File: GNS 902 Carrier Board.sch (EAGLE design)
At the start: 8 parts, among them U1 GNS-902

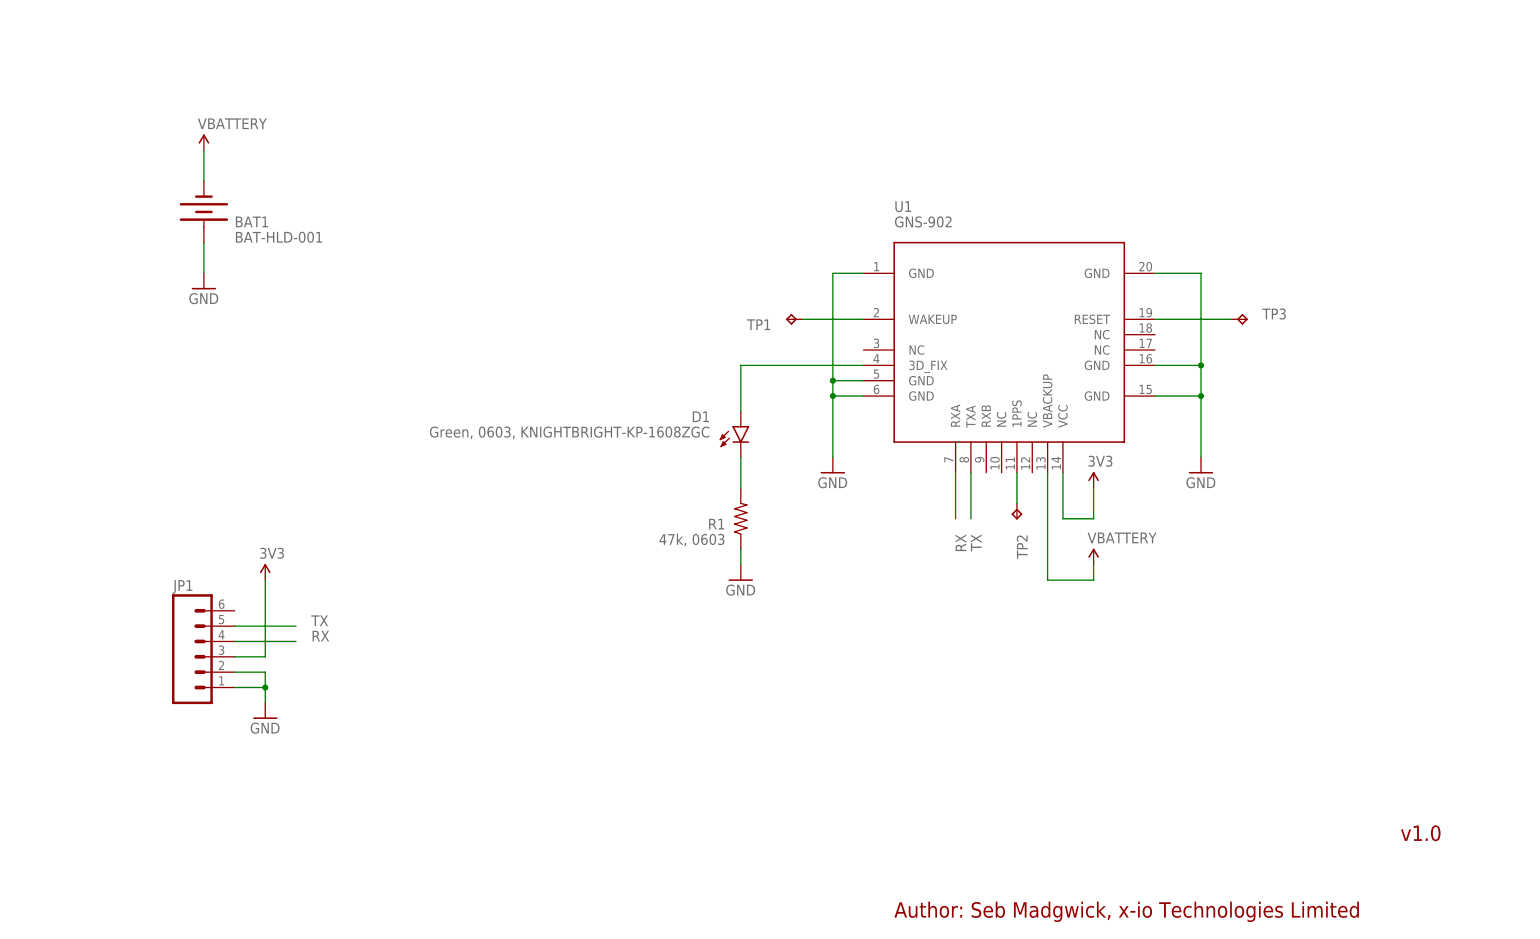
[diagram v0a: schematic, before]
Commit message: Add automatic VBACKUP power source switch
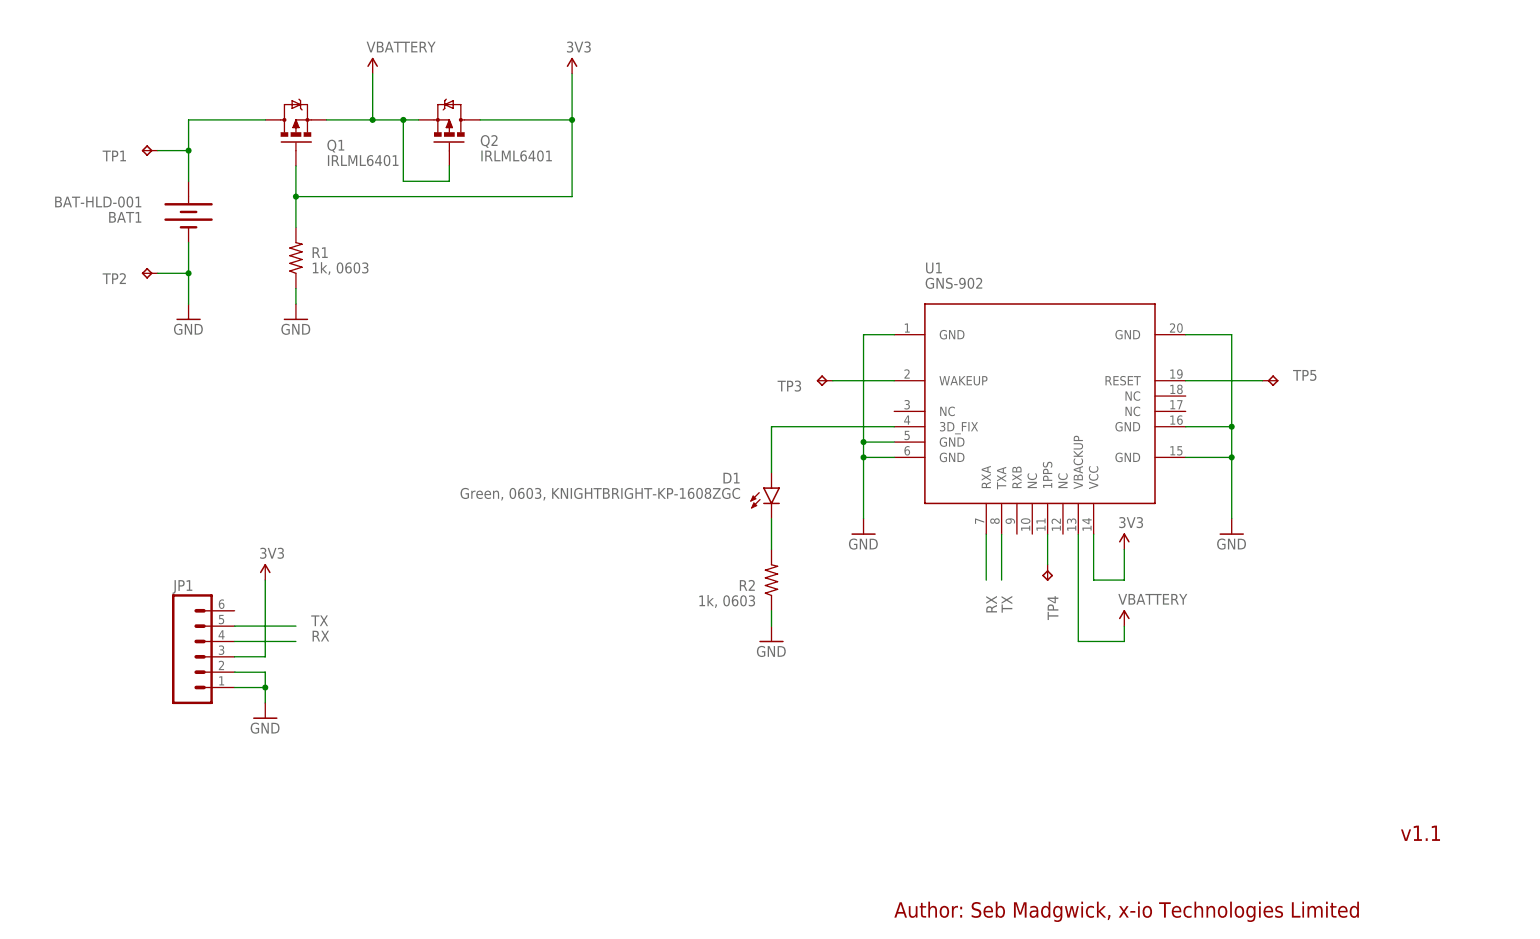
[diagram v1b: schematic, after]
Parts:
- added Q1, Q2: IRLML6401, SparkFun-DiscreteSemi:MOSFET-PCHANNEL
- added R2: 1k, 0603, SparkFun-Resistors:RESISTOR0603
- added TP4, TP5: TPTP10R, testpad:TPTP10R
- R1: value 47k, 0603 -> 1k, 0603
- TP1, TP2: value TPTP10R -> TPTP15R; device testpad:TPTP10R -> testpad:TPTP15R
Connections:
- new net N$6: BAT1.+, Q1.D, TP1.TP
- net 3V3: now also Q1.G, Q2.D, R1.2
- net GND: now also BAT1.-, R2.1, TP2.TP; no longer BAT1.+
- net N$2: now also R2.2; no longer R1.2
- net N$3: now also TP3.TP; no longer TP1.TP
- net N$4: now also TP4.TP; no longer TP2.TP
- net N$5: now also TP5.TP; no longer TP3.TP
- net VBATTERY: now also Q1.S, Q2.G, Q2.S; no longer BAT1.-
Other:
- note added: "v1.1"
- note removed: "v1.0"
- moved on the sheet: BAT1, D1, R1, TP1, TP2, TP3, U1

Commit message: Correct GNS-902 footprint and add notes to schematic
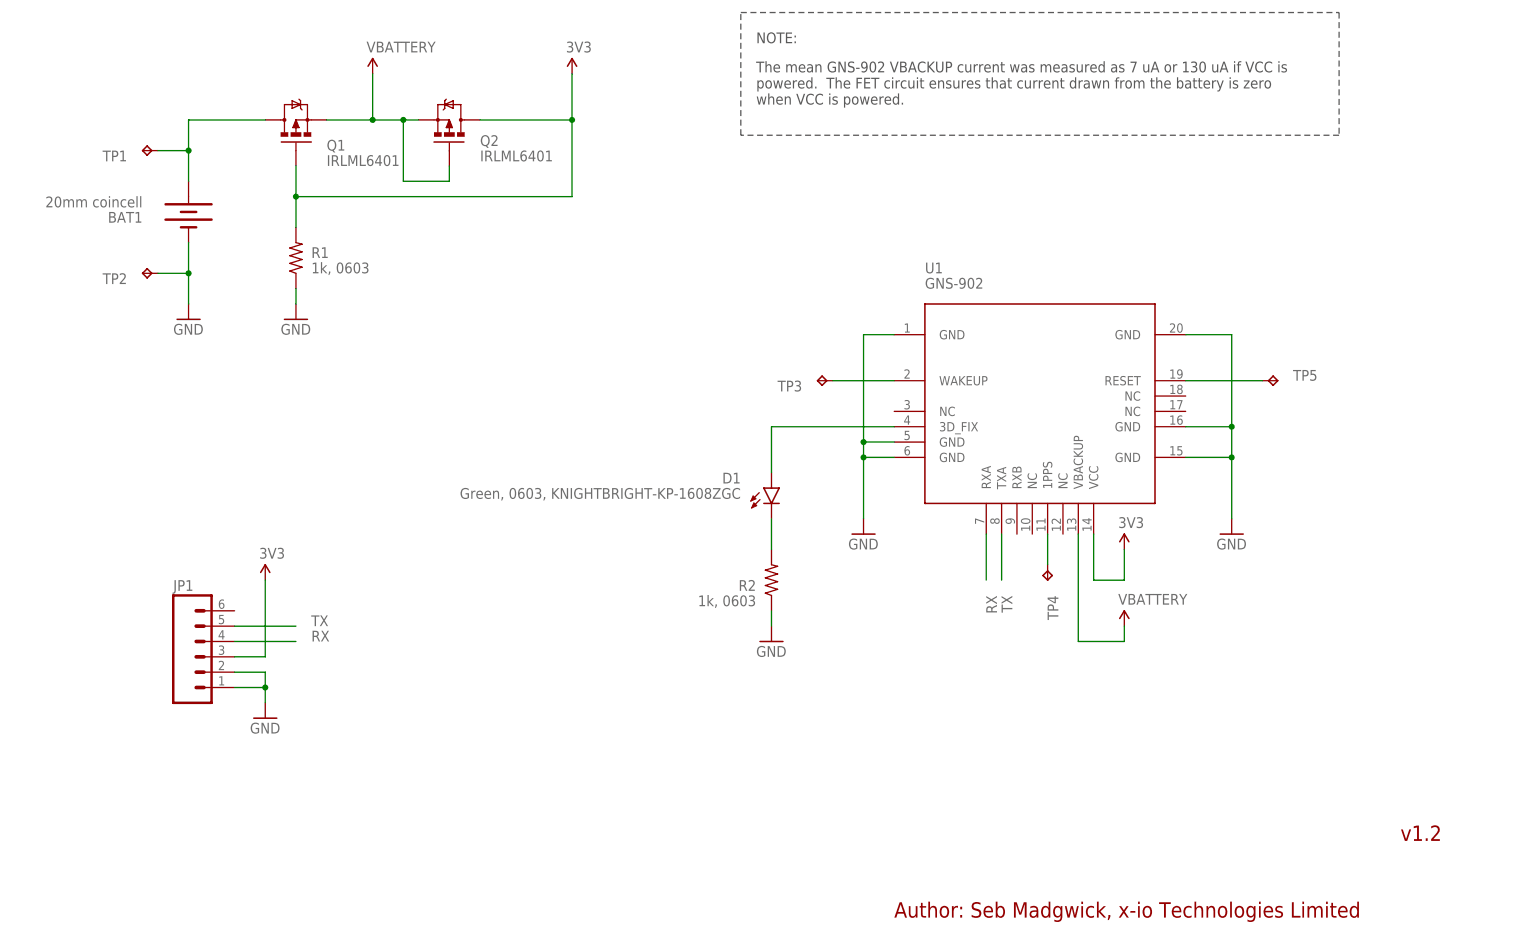
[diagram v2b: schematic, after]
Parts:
- BAT1: value BAT-HLD-001 -> 20mm coincell
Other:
- note added: "NOTE:"
- note added: "The mean GNS-902 VBACKUP current was measured as 7 uA or 130 uA if VCC is powered. The FET circuit ensures that current drawn from the battery is zero when VCC is powered."
- note added: "v1.2"
- note removed: "v1.1"
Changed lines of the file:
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@@
 <part name="GND5" library="SparkFun-Aesthetics" deviceset="GND" device=""/>
 <part name="GND6" library="SparkFun-Aesthetics" deviceset="GND" device=""/>
-<part name="BAT1" library="SparkFun-Electromechanical" deviceset="BATTERY" device="20MM_4LEGS" value="BAT-HLD-001"/>
+<part name="BAT1" library="SparkFun-Electromechanical" deviceset="BATTERY" device="20MM_4LEGS" value="20mm coincell"/>
 <part name="GND1" library="SparkFun-Aesthetics" deviceset="GND" device=""/>
 <part name="JP1" library="SparkFun-Connectors" deviceset="M06" device="NO_SILK_FEMALE_PTH"/>
@@
 <sheet>
 <plain>
-<text x="246.38" y="20.32" size="2.54" layer="94">v1.1</text>
+<text x="246.38" y="20.32" size="2.54" layer="94">v1.2</text>
 <text x="162.56" y="7.62" size="2.54" layer="94">Author: Seb Madgwick, x-io Technologies Limited</text>
+<text x="139.7" y="142.24" size="1.778" layer="97">The mean GNS-902 VBACKUP current was measured as 7 uA or 130 uA if VCC is
+powered.  The FET circuit ensures that current drawn from the battery is zero
+when VCC is powered.</text>
+<text x="139.7" y="152.4" size="1.778" layer="97">NOTE:</text>
+<wire x1="137.16" y1="157.48" x2="236.22" y2="157.48" width="0.1524" layer="97" style="shortdash"/>
+<wire x1="236.22" y1="157.48" x2="236.22" y2="137.16" width="0.1524" layer="97" style="shortdash"/>
+<wire x1="236.22" y1="137.16" x2="137.16" y2="137.16" width="0.1524" layer="97" style="shortdash"/>
+<wire x1="137.16" y1="137.16" x2="137.16" y2="157.48" width="0.1524" layer="97" style="shortdash"/>
 </plain>
 <instances>
@@
 </schematic>
 </drawing>
+<compatibility>
+<note version="6.3" minversion="6.2.2" severity="warning">
+Since Version 6.2.2 text objects can contain more than one line,
+which will not be processed correctly with this version.
+</note>
+</compatibility>
 </eagle>
